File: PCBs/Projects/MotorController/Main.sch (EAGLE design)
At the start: 29 parts, among them Q1 ZXMP10A17GQ, Q2 BUK9240-100A.118, Q3 BUK9240-100A.118, Q4 MMBT5551LT1G, U1 LT4356-2

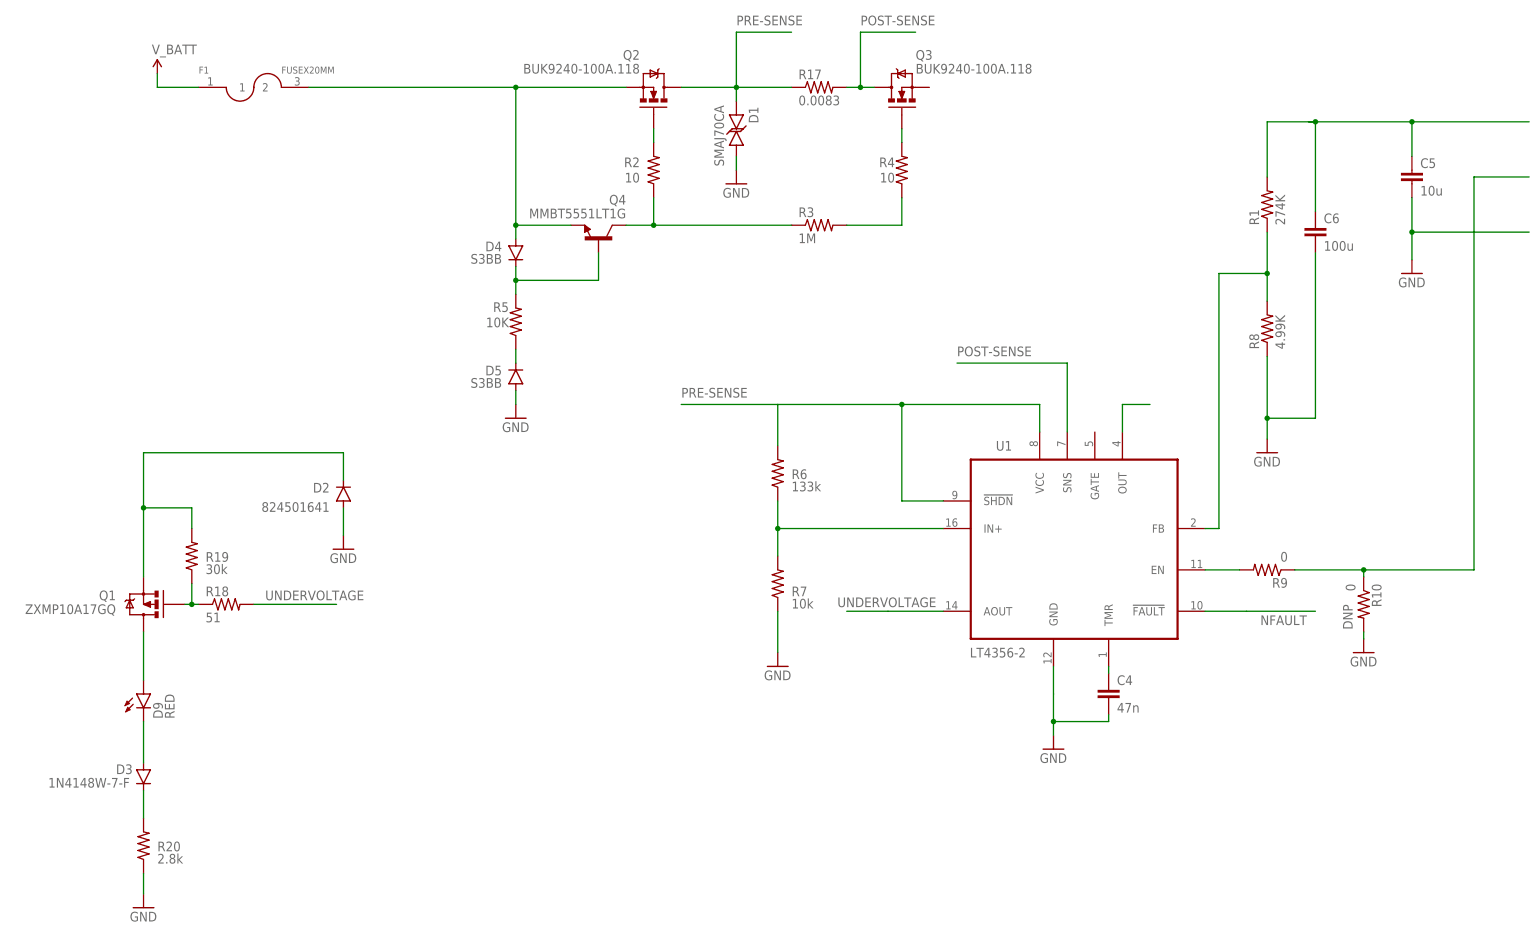
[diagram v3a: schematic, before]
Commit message: Finished input protection sheet
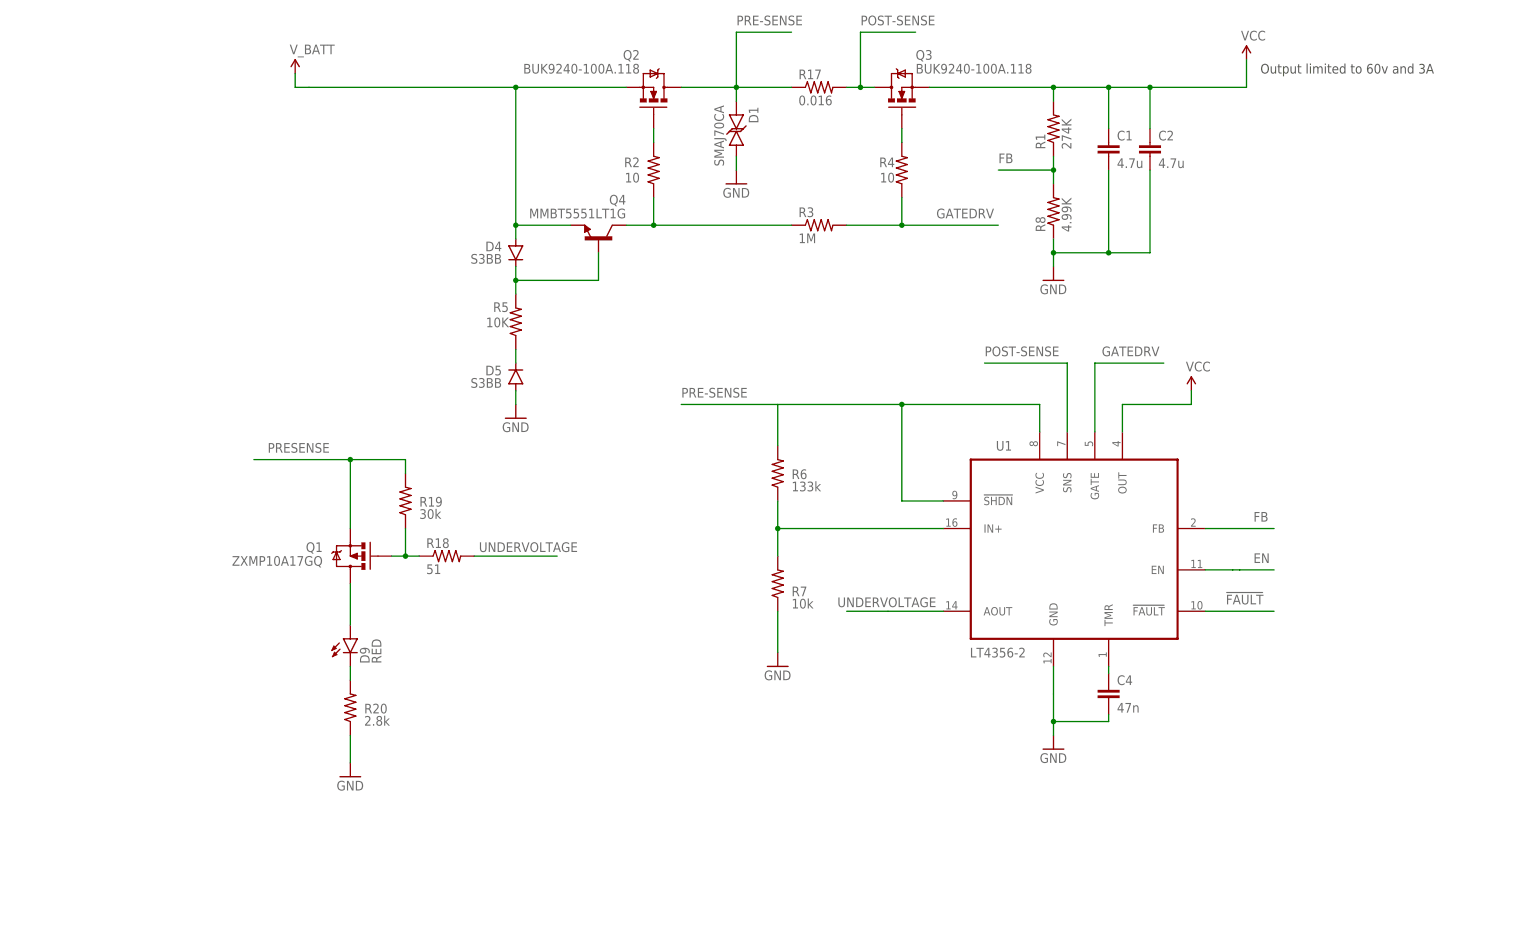
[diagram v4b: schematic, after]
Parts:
- removed C5: 10u, SparkFun-Capacitors:CAP1210
- removed C6: 100u, SparkFun-Capacitors:CAP1210
- removed D2: 824501641, SparkFun-DiscreteSemi:DIODESMA-ALT
- removed D3: 1N4148W-7-F, SparkFun-DiscreteSemi:DIODESOD123
- removed F1: FUSEX20MM, SparkFun-Passives:FUSEX20MM
- removed R10, R9: 0, SparkFun-Resistors:RESISTOR0805-RES
- added C1, C2: 4.7u, SparkFun-Passives:CAP1210
- R17: value 0.0083 -> 0.016
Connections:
- net N$14 renamed FB
- net NFAULT renamed !FAULT
- removed net N$15: R10.1, R9.1
- removed net N$16: D3.C, R20.2
- removed net N$2: R9.2, U1.EN
- removed net N$21: R3.2, R4.1
- removed net N$3: C5.1, C6.1, R1.2
- removed net N$5: U1.OUT
- removed net N$6: D2.C, Q1.S, R19.2
- removed net V_BATT: F1.1
- new net EN: U1.EN
- new net GATEDRV: R3.2, R4.1, U1.GATE
- new net PRESENSE: Q1.S, R19.2
- new net VCC: C1.1, C2.1, Q3.S, R1.2, U1.OUT
- net GND: now also C1.2, C2.2; no longer C5.2, C6.2, D2.A, R10.2
- net N$4: now also R20.2; no longer D3.A
- net N$8: no longer F1.2
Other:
- note added: "Output limited to 60v and 3A"
- moved on the sheet: D9, Q1, R1, R18, R19, R20, R8

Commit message: gate driver halfway cleaned up
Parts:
- added C10, C17: 4.7u, SparkFun-Capacitors:CAP1210
- added C11, C16, C8: 0.1u, SparkFun-Capacitors:CAP0805
- added C12, C13: 47u, SparkFun-Capacitors:CAP1210
- added C14, C9: 22n, SparkFun-Capacitors:CAP0805
- added C15: 2.2u, SparkFun-Capacitors:CAP1210
- added C21, C22, C23: 0.1u, SparkFun-Passives:CAPPTH
- added C3: 120P, SparkFun-Capacitors:CAP0805
- added C5: 6.8N, SparkFun-Capacitors:CAP0805
- added C6, C7: 1u, SparkFun-Capacitors:CAP0805
- added D2: PMEG10030ELPX, SparkFun-DiscreteSemi:PMEG10030ELPX
- added L1: 22u, SparkFun-Passives:INDUCTORPWR
- added R10: 250k, SparkFun-Resistors:RESISTORPTH-1/4W-VERT
- added R11: 100, SparkFun-Resistors:RESISTORPTH-1/4W-VERT
- added R12: 10k, SparkFun-Resistors:RESISTORPTH-1/4W-VERT
- added R13: 51k, SparkFun-Resistors:RESISTORPTH-1/4W-VERT
- added R9: 16.2K, SparkFun-Resistors:RESISTORPTH-1/4W-VERT
- added U2: DRV8301, IC:DRV8301
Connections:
- removed net EN: U1.EN
- new net !CS: U2.!SCS
- new net !OCTW: U2.!OCTW
- new net 5V: C12.1, C13.1, L1.2, R13.2
- new net A: C21.2, U2.SH_A
- new net B: C22.2, U2.SH_B
- new net BUCK-EN: U1.EN, U2.EN_BUCK
- new net C: C23.2, U2.SH_C
- new net EN_GATE: U2.EN_GATE
- new net GH_A: U2.GH_A
- new net GH_B: U2.GH_B
- new net GH_C: U2.GH_C
- new net GL_A: U2.GL_A
- new net GL_B: U2.GL_B
- new net GL_C: U2.GL_C
- new net INH_A: U2.INH_A
- new net INH_B: U2.INH_B
- new net INH_C: U2.INH_C
- new net INL_A: U2.INL_A
- new net INL_B: U2.INL_B
- new net INL_C: U2.INL_C
- new net MISO: U2.SDO
- new net MOSI: U2.SDI
- new net N$10: C7.1, U2.AVDD
- new net N$12: C9.1, U2.SS_TR
- new net N$14: R12.2, R13.1, U2.VSENSE
- new net N$15: C11.1, U2.BST_BK
- new net N$16: C11.2, D2.C, L1.1, U2.PH
- new net N$17: C14.2, U2.CP2
- new net N$18: C14.1, U2.CP1
- new net N$2: R10.2, U2.RT_CLK
- new net N$21: C15.1, U2.GVDD
- new net N$24: C21.1, U2.BST_A
- new net N$25: C23.1, U2.BST_C
- new net N$26: R11.1, U2.DTC
- new net N$3: C5.1, R9.2
- new net N$30: C22.1, U2.BST_B
- new net N$31: U2.VDD_SPI
- new net N$5: C6.1, U2.DVDD
- new net N$6: C3.1, R9.1, U2.COMP
- new net PWRGD: U2.PWRGD
- new net SCLK: U2.SCLK
- new net SN1: U2.SN1
- new net SN2: U2.SN2
- new net SP1: U2.SP1
- new net SP2: U2.SP2
- new net VDD: C10.1, C16.1, C17.2, C8.1, U2.PVDD1, U2.PVDD2
- net !FAULT: now also U2.!FAULT
- net GND: now also C10.2, C12.2, C13.2, C15.2, C16.2, C17.1, C3.2, C5.2, C6.2, C7.2, C8.2, C9.2, D2.A, R10.1, R11.2, R12.1, U2.AGND, U2.GND(EXP_PAD), U2.SL_A, U2.SL_B, U2.SL_C

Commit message: Gate driver completed
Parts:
- added FRAME1, FRAME2: FRAME-LEDGER, SparkFun-Aesthetics:FRAME-LEDGER
- added R14: 47k, SparkFun-Resistors:RESISTORPTH-1/4W-VERT
- added U3: LT1963A-3.3, SparkFun-PowerIC:LT1963A-3.3
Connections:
- removed net N$31: U2.VDD_SPI
- new net 3.3V: U2.VDD_SPI, U3.OUT, U3.SENSE/ADJ
- net 5V: now also R14.2, U3.IN
- net GND: now also U3.GND@3, U3.GND@6, U3.GND@7
- net PWRGD: now also R14.1, U3.!SHDN
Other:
- note added: "Input Protection"
- moved on the sheet: C1, C10, C11, C12, C13, C14, C15, C16, C17, C2, C21, C22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

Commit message: Added power fet part and start of psoc5lp part -further schematic cleaning done on the gate driver -datasheet for some of the new parts have been added
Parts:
- added FRAME3, FRAME4: FRAME-LEDGER, SparkFun-Aesthetics:FRAME-LEDGER
- added U4: MTI85W100GC, IC:MTI85W100GC
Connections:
- removed net VDD: C10.1, C16.1, C17.2, C8.1, U2.PVDD1, U2.PVDD2
- net VCC: now also C10.1, C16.1, C17.2, C8.1, U2.PVDD1, U2.PVDD2
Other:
- note added: "Gate Driver and Power Supply"

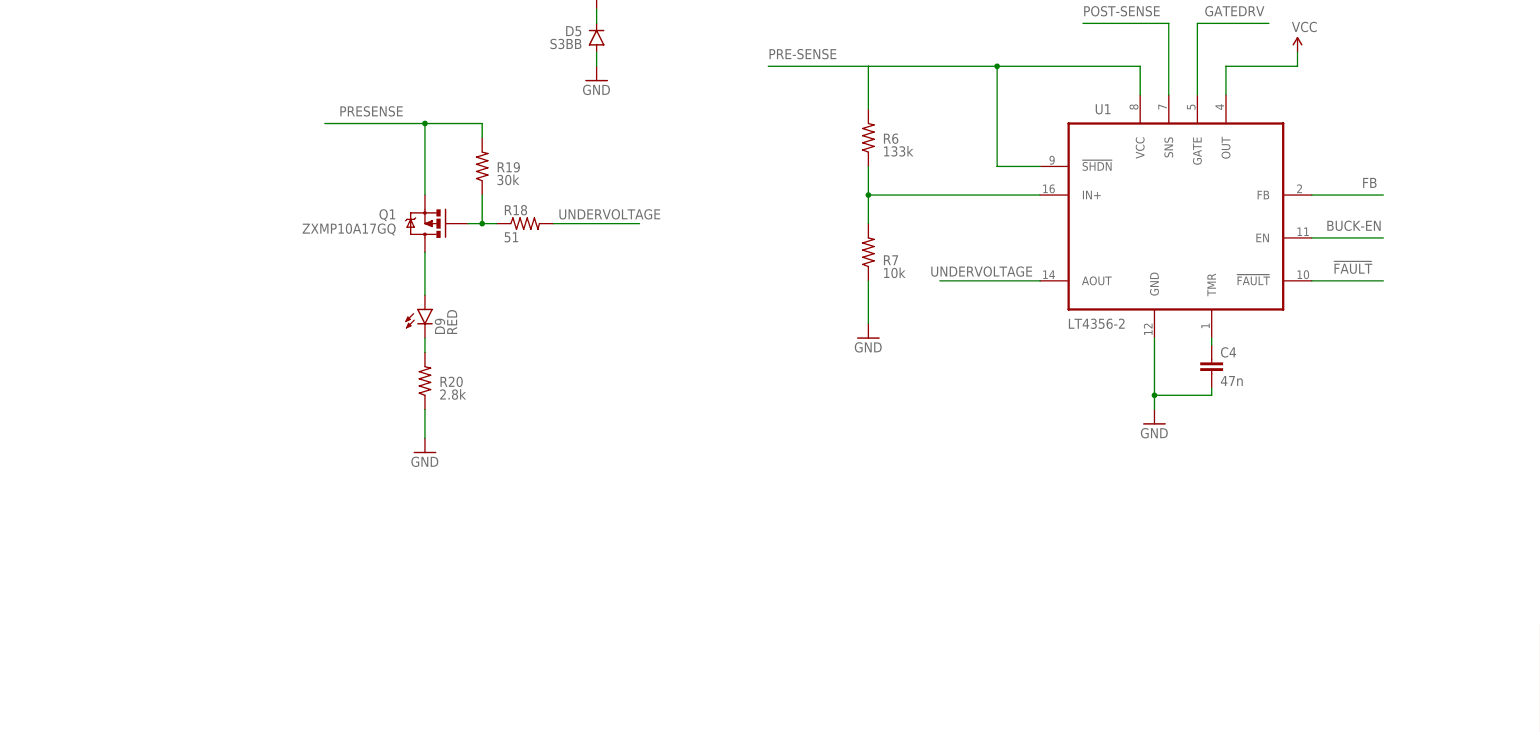
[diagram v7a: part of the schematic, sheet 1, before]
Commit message: Freewheeling diodes selected and mcu created -documentation for fet module corrected -minor symbol changes
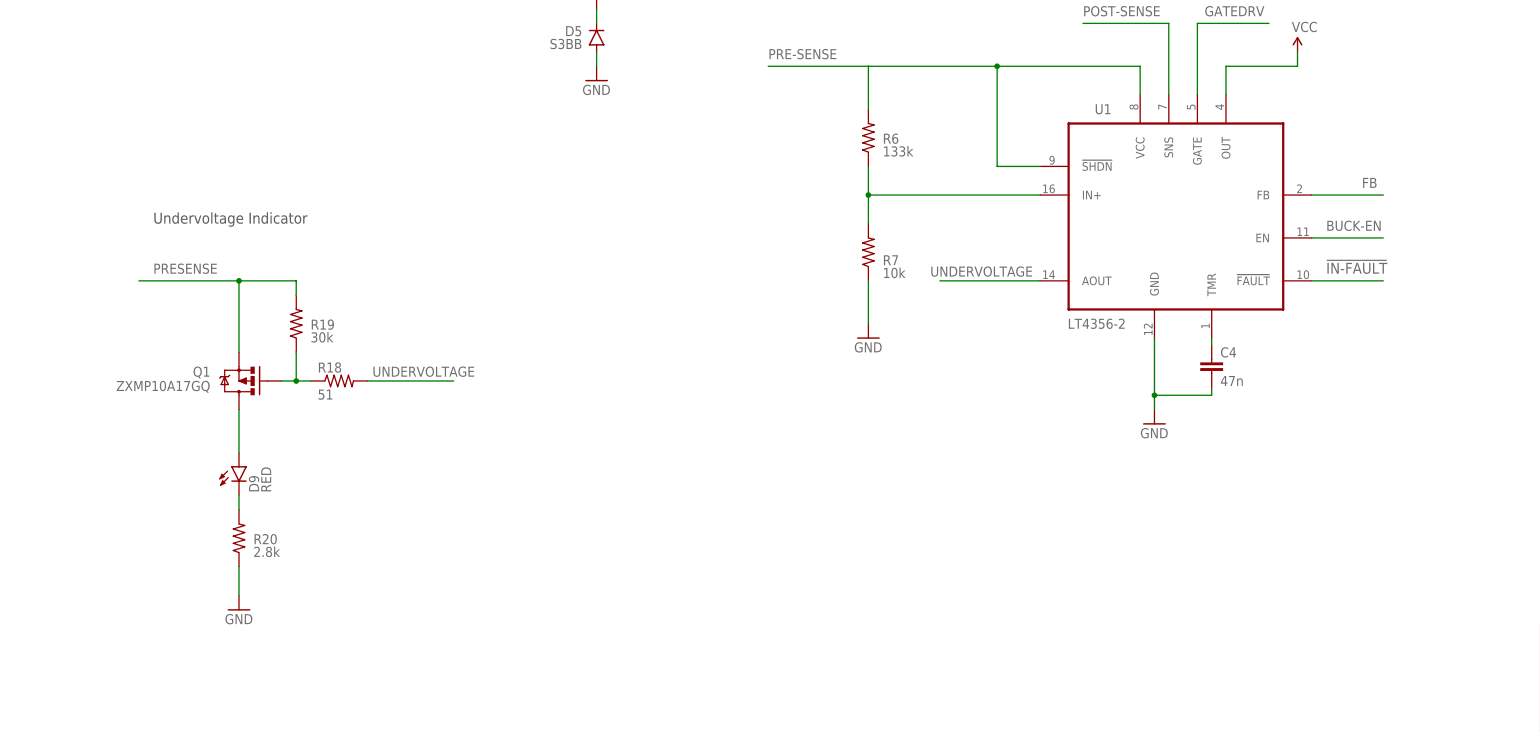
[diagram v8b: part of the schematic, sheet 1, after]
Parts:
- removed C23: 0.1u, SparkFun-Passives:CAPPTH
- added C18: 10u, SparkFun-Capacitors:CAP1210
- added C19: 22n, SparkFun-Capacitors:CAP0805
- added C20: 0.1u, SparkFun-Capacitors:CAP0805
- added D10, D11, D3, D6, D7, D8: MBRF1090, SparkFun-DiscreteSemi:DIODE-SCHOTTKY-B340A
- added MOD1: PSOC5LP-DEVBRD, modules:PSOC5LP-DEVBRD
- C21, C22: device SparkFun-Passives:CAPPTH -> SparkFun-Capacitors:CAP0805
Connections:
- new net !IN-FAULT: U1.!FAULT
- new net N$27: U4.L+
- new net N$28: D11.C, D6.C, D7.C
- new net N$31: D7.A, D8.C
- net !FAULT: no longer U1.!FAULT
- net 3.3V: now also C18.1, C19.1, MOD1.VDD, MOD1.VDDIO
- net A: now also C22.2, D3.C, D6.A, U4.L1; no longer C21.2
- net B: now also C21.2, U4.L2; no longer C22.2
- net C: now also C20.2, D10.C, D11.A, U4.L3; no longer C23.2
- net GND: now also C18.2, C19.2, D10.A, D3.A, D8.A, MOD1.GND, U4.L-
- net N$24: now also C22.1; no longer C21.1
- net N$25: now also C20.1; no longer C23.1
- net N$30: now also C21.1; no longer C22.1
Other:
- note added: "Microcontroller"
- note added: "Undervoltage Indicator"
- moved on the sheet: C21, C22, D9, Q1, R18, R19, R20
